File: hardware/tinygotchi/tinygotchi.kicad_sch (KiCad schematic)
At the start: 27 parts, among them J1 Conn_01x02, J2 USB_C_Receptacle, J3 S2B-PH-SM4-TB, Q1 FN340P, SW1 LEFT, SW2 MID, SW3 RIGHT, U1 ATtiny3227-M, U2 OLED_Module, U3 TP4056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

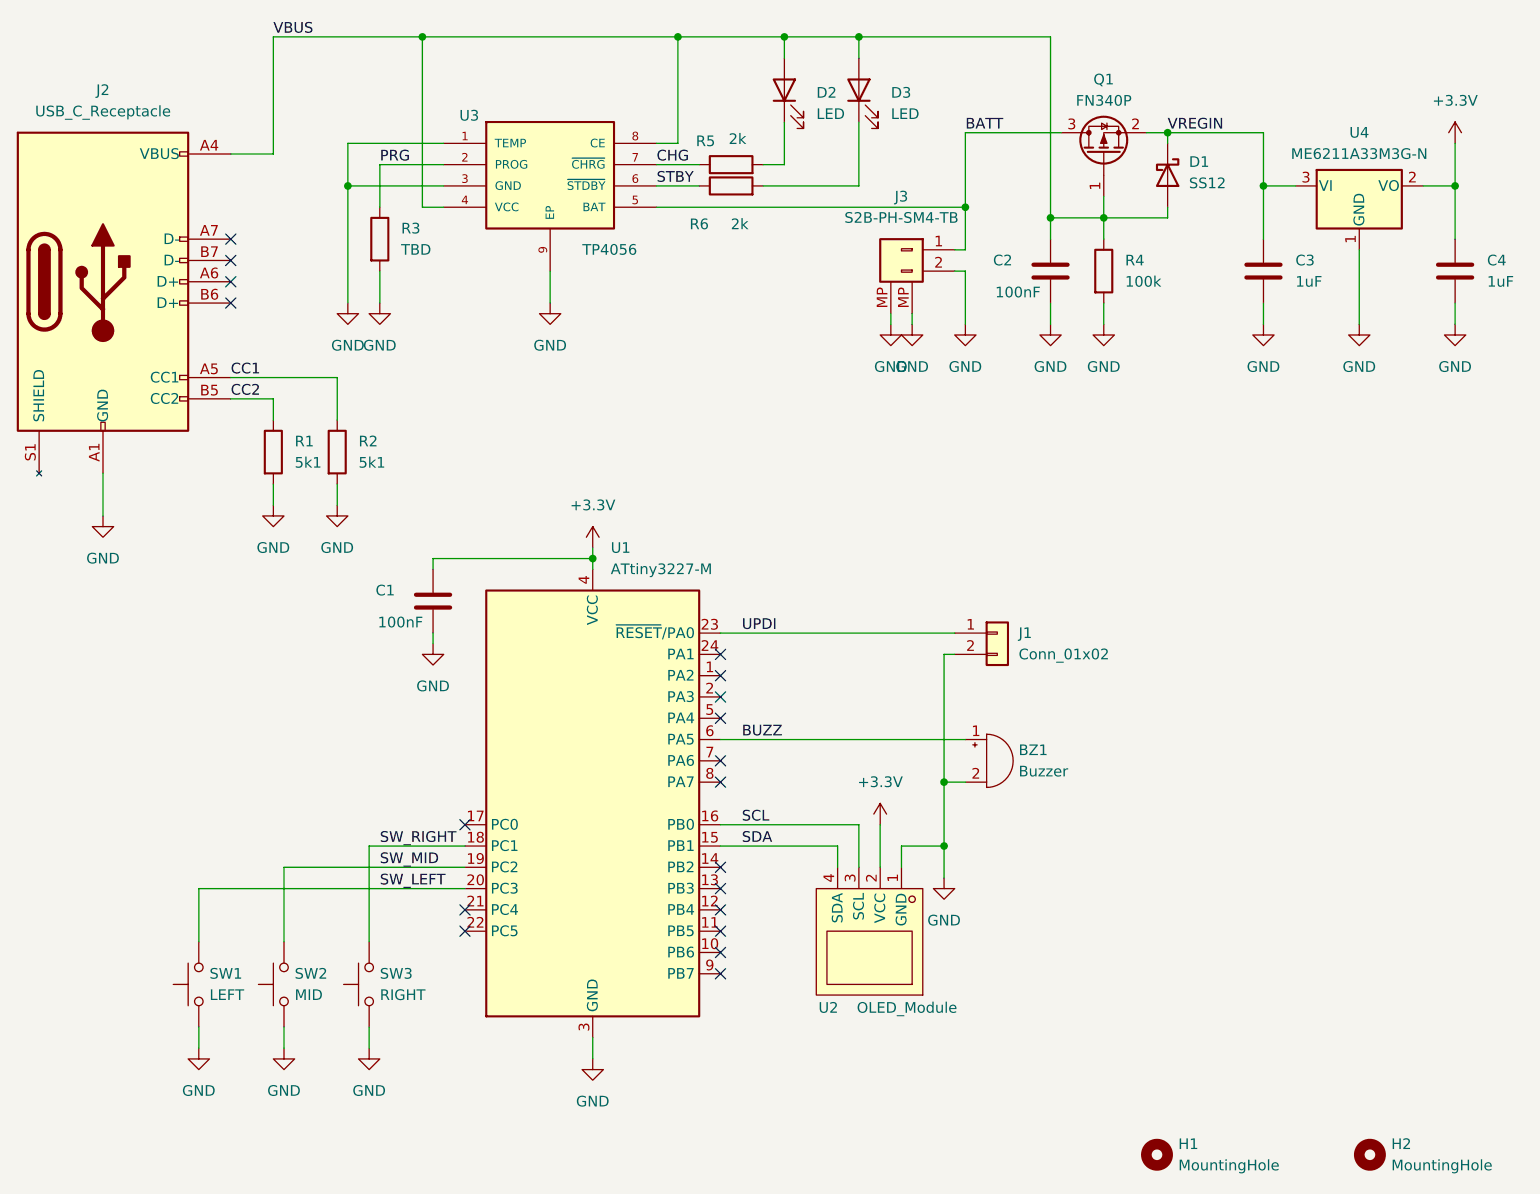
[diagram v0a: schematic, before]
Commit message: update shematic and PCB edge cut
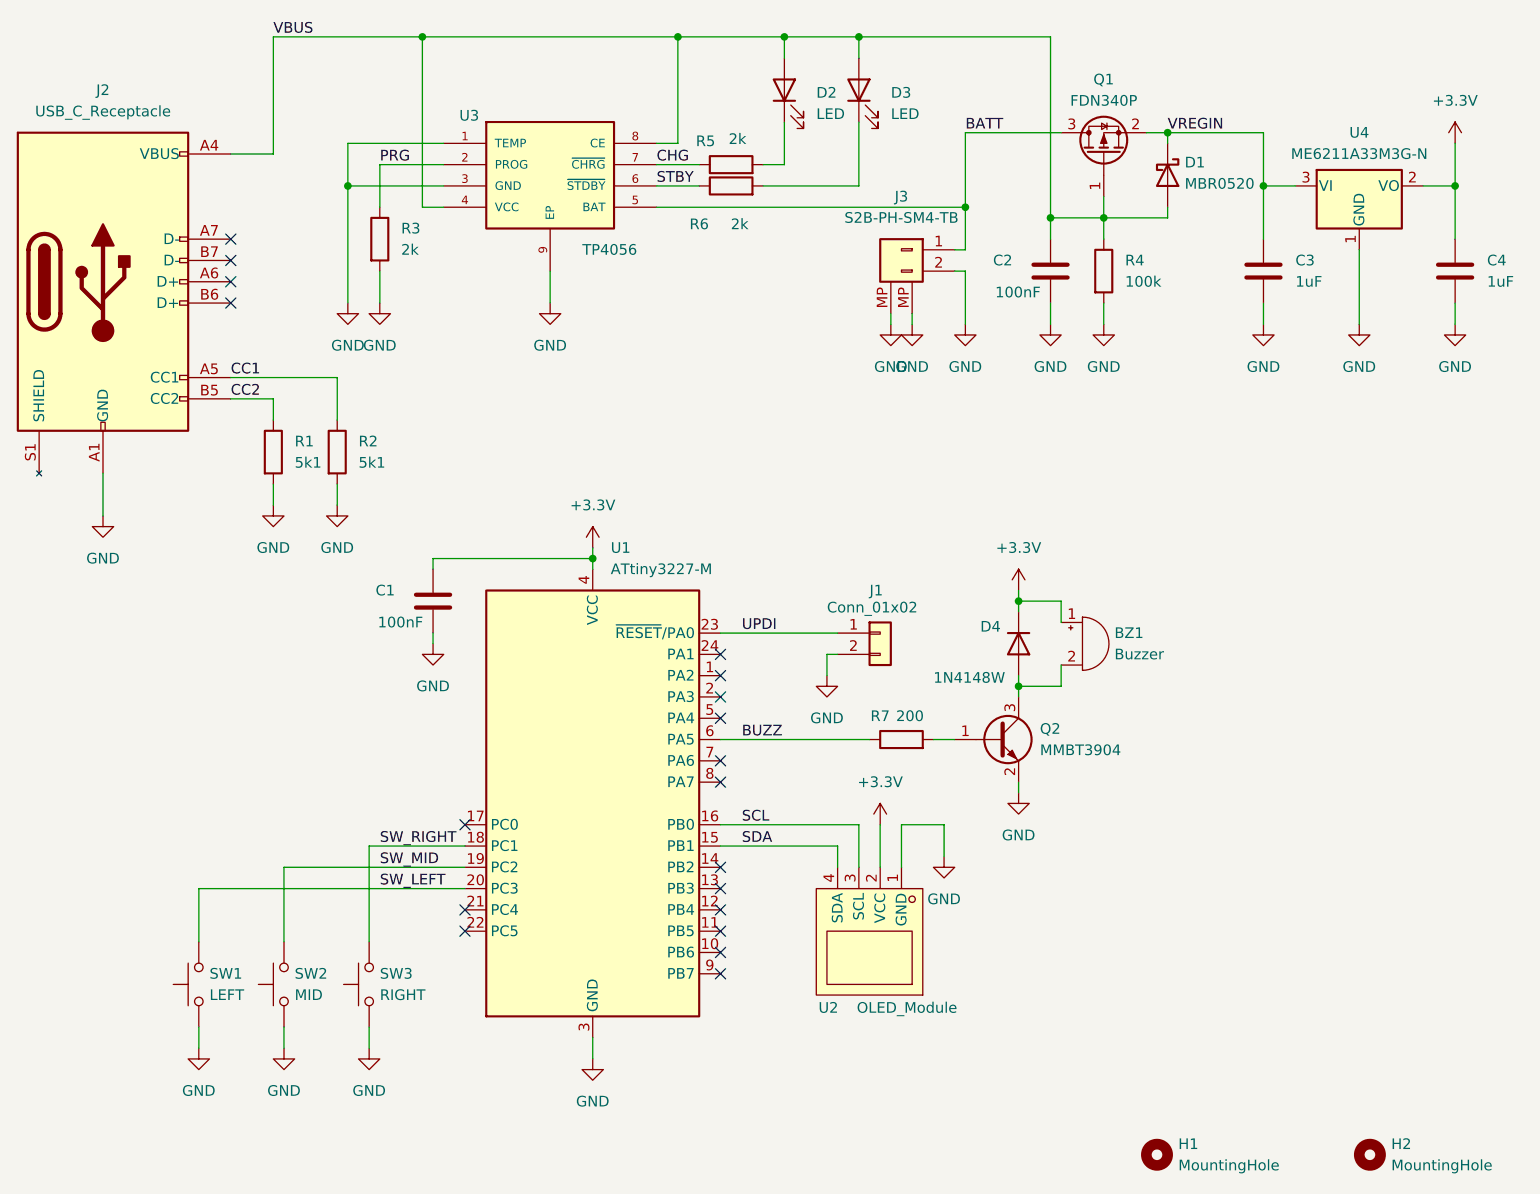
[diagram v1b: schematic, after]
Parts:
- added D4: 1N4148W, Diode_SMD:D_SOD-123, symbol Diode:1N4148WT
- added Q2: MMBT3904, Package_TO_SOT_SMD:SOT-23, symbol Transistor_BJT:MMBT3904
- added R7: 200, Resistor_SMD:R_0603_1608Metric, symbol Device:R
- BZ1: footprint (none) -> my_lbrary:FUET-5030-BUZZER
- C1, C2, C3, C4: footprint (none) -> Capacitor_SMD:C_0603_1608Metric
- D1: value SS12 -> MBR0520; footprint (none) -> Diode_SMD:D_SOD-123
- D2, D3: footprint (none) -> LED_SMD:LED_0603_1608Metric
- H1, H2: footprint (none) -> MountingHole:MountingHole_2.2mm_M2
- Q1: value FN340P -> FDN340P; footprint (none) -> Package_TO_SOT_SMD:SOT-23
- R1, R2, R4, R5, R6: footprint (none) -> Resistor_SMD:R_0603_1608Metric
- R3: value TBD -> 2k; footprint (none) -> Resistor_SMD:R_0603_1608Metric
- SW1, SW2, SW3: footprint (none) -> my_lbrary:SW_PUSH_6mm_XKB_TS-1102SD-X-X-X
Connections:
- net +3.3V: now also BZ1.1 (+), D4.1 (K)
- net BUZZ: now also R7.1; no longer BZ1.1 (+)
- net GND: now also Q2.2 (E); no longer BZ1.2 (-)
- new net: Q2.1 (B), R7.2
- new net: BZ1.2 (-), D4.2 (A), Q2.3 (C)
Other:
- title: tinyGotChi Schematic -> tinygotchi Schematic
- moved on the sheet: BZ1, J1
